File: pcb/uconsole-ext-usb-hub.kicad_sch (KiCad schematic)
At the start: 33 parts, among them J1 MINI_PCIE, P1 USB_C_Plug_USB2.0, P2 USB_C_Plug_USB2.0, P3 USB_C_Plug_USB2.0, P4 USB_C_Plug_USB2.0, U1 TUSB2048B, U2 TPS2044D, U3 USBLC6-2P6, U4 USBLC6-2P6, U5 USBLC6-2P6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

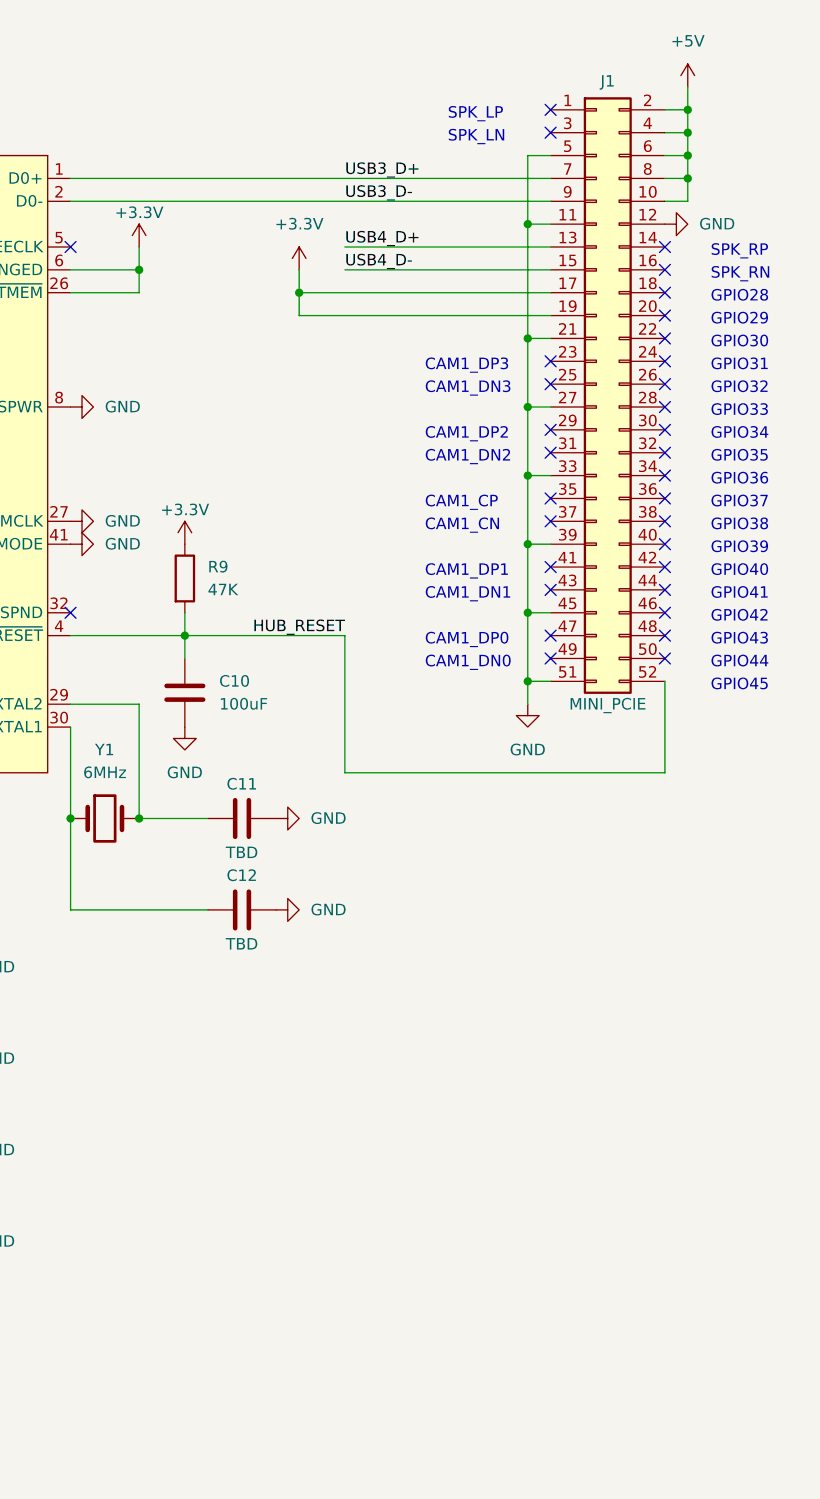
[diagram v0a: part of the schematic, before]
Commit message: sch: add speakers
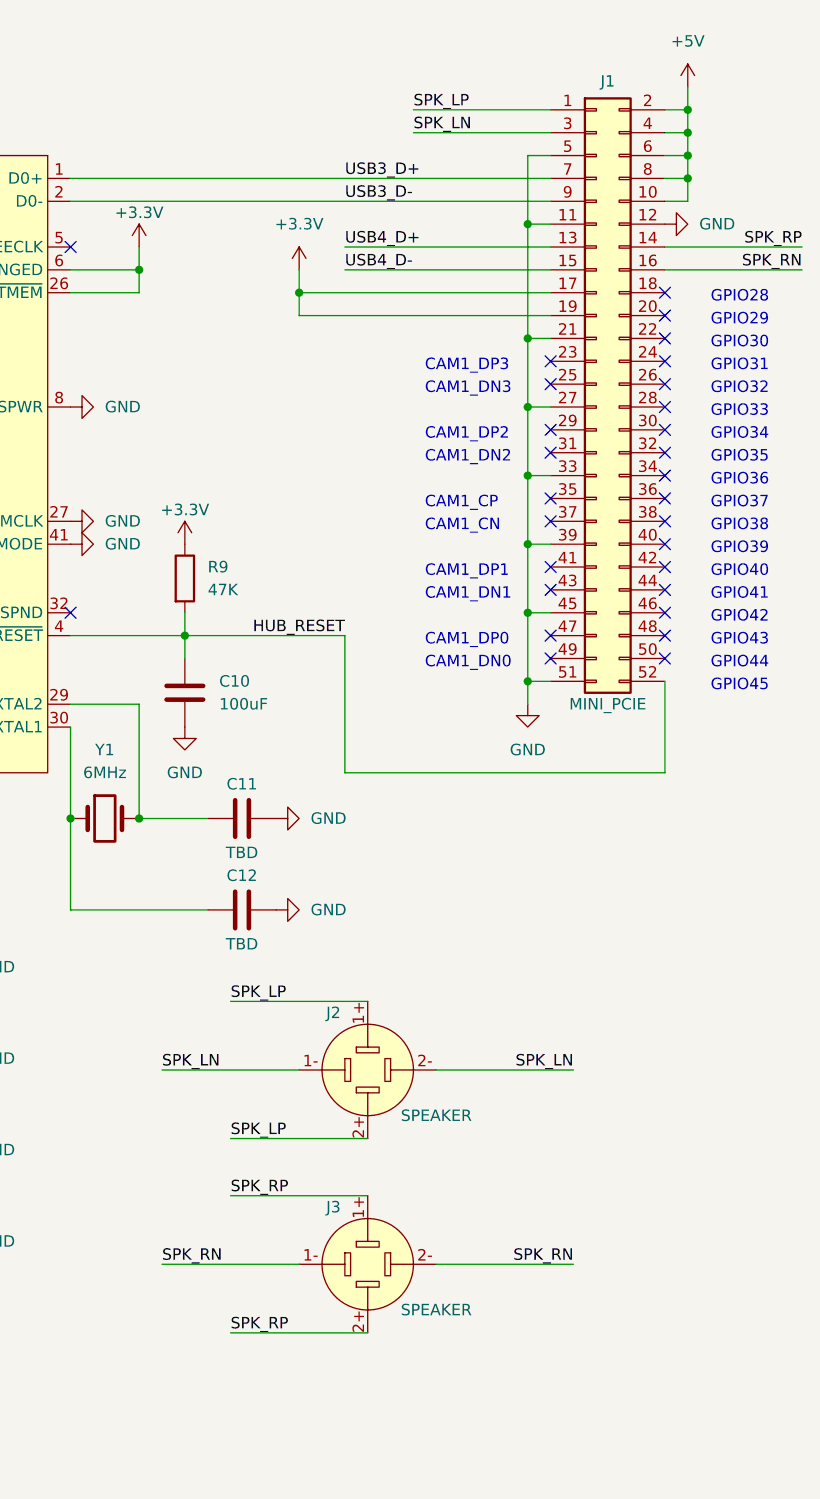
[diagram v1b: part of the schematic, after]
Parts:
- added J2, J3: SPEAKER, symbol Connector_Audio:SpeakON_NL4
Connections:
- net SPK_LP: now reaches J1.1 (Pin_1)
- net SPK_LP: now also J2.1+, J2.2+
- net SPK_RP: now reaches J1.14 (Pin_14)
- net SPK_RP: now also J3.1+, J3.2+
- net SPK_RN: now reaches J1.16 (Pin_16)
- net SPK_RN: now also J3.1-, J3.2-
- net SPK_LN: now reaches J1.3 (Pin_3)
- net SPK_LN: now also J2.1-, J2.2-
- no-connect marks 33 -> 29
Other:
- note removed: "SPK_LN"
- note removed: "SPK_LP"
- note removed: "SPK_RN"
- note removed: "SPK_RP"
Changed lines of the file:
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@@
   (title_block
     (title "uConsole Extension USB Hub")
-    (date "2023-07-21")
-    (rev "0.0.1")
+    (date "2023-07-22")
+    (rev "0.0.2")
     (company "by argrento")
     (comment 2 "https://codeberg.org/argrento/uconsole-ext-usb-hub")
@@
   (junction (at 254 86.36) (diameter 0) (color 0 0 0 0)
   )
-  (no_connect (at 269.24 40.64))
-  (no_connect (at 269.24 38.1))
   (no_connect (at 269.24 81.28))
   (no_connect (at 269.24 55.88))
@@
   (no_connect (at 256.54 68.58))
   (no_connect (at 256.54 60.96))
-  (no_connect (at 256.54 25.4))
   (no_connect (at 269.24 68.58))
-  (no_connect (at 256.54 22.86))
   (no_connect (at 269.24 63.5))
   (no_connect (at 269.24 83.82))
@@
     (stroke (width 0) (type default))
   )
+  (wire (pts (xy 241.3 25.4) (xy 256.54 25.4))
+    (stroke (width 0) (type default))
+  )
   (wire (pts (xy 165.1 91.44) (xy 165.1 165.1))
     (stroke (width 0) (type default))
@@
     (stroke (width 0) (type default))
   )
+  (wire (pts (xy 241.3 22.86) (xy 256.54 22.86))
+    (stroke (width 0) (type default))
+  )
   (wire (pts (xy 187.96 20.32) (xy 190.5 20.32))
     (stroke (width 0) (type default))
@@
     (stroke (width 0) (type default))
   )
+  (wire (pts (xy 259.08 151.13) (xy 243.84 151.13))
+    (stroke (width 0) (type default))
+  )
   (wire (pts (xy 53.34 128.27) (xy 39.37 128.27))
     (stroke (width 0) (type default))
@@
     (stroke (width 0) (type default))
   )
+  (wire (pts (xy 220.98 143.51) (xy 236.22 143.51))
+    (stroke (width 0) (type default))
+  )
   (wire (pts (xy 67.31 22.86) (xy 67.31 25.4))
     (stroke (width 0) (type default))
@@
     (stroke (width 0) (type default))
   )
+  (wire (pts (xy 284.48 40.64) (xy 269.24 40.64))
+    (stroke (width 0) (type default))
+  )
   (wire (pts (xy 203.2 91.44) (xy 203.2 101.6))
     (stroke (width 0) (type default))
@@
     (stroke (width 0) (type default))
   )
+  (wire (pts (xy 220.98 158.75) (xy 236.22 158.75))
+    (stroke (width 0) (type default))
+  )
   (wire (pts (xy 53.34 168.91) (xy 39.37 168.91))
     (stroke (width 0) (type default))
@@
     (stroke (width 0) (type default))
   )
+  (wire (pts (xy 213.36 129.54) (xy 228.6 129.54))
+    (stroke (width 0) (type default))
+  )
   (wire (pts (xy 254 35.56) (xy 254 48.26))
     (stroke (width 0) (type default))
@@
     (stroke (width 0) (type default))
   )
+  (wire (pts (xy 220.98 137.16) (xy 236.22 137.16))
+    (stroke (width 0) (type default))
+  )
   (wire (pts (xy 137.16 132.08) (xy 152.4 132.08))
     (stroke (width 0) (type default))
@@
     (stroke (width 0) (type default))
   )
+  (wire (pts (xy 213.36 151.13) (xy 228.6 151.13))
+    (stroke (width 0) (type default))
+  )
   (wire (pts (xy 24.13 194.31) (xy 31.75 194.31))
     (stroke (width 0) (type default))
   )
+  (wire (pts (xy 220.98 121.92) (xy 236.22 121.92))
+    (stroke (width 0) (type default))
+  )
   (wire (pts (xy 142.24 91.44) (xy 142.24 60.96))
     (stroke (width 0) (type default))
@@
     (stroke (width 0) (type default))
   )
+  (wire (pts (xy 259.08 129.54) (xy 243.84 129.54))
+    (stroke (width 0) (type default))
+  )
   (wire (pts (xy 116.84 91.44) (xy 142.24 91.44))
     (stroke (width 0) (type default))
@@
     (stroke (width 0) (type default))
   )
+  (wire (pts (xy 284.48 38.1) (xy 269.24 38.1))
+    (stroke (width 0) (type default))
+  )
   (text "CAM1_DN1" (at 242.57 77.47 0)
     (effects (font (size 1.27 1.27)) (justify left bottom))
@@
     (effects (font (size 1.27 1.27)) (justify left bottom))
   )
-  (text "SPK_RN" (at 274.32 41.91 0)
-    (effects (font (size 1.27 1.27)) (justify left bottom))
-  )
   (text "CAM1_DP3" (at 242.57 52.07 0)
     (effects (font (size 1.27 1.27)) (justify left bottom))
@@
     (effects (font (size 1.27 1.27)) (justify left bottom))
   )
-  (text "SPK_RP" (at 274.32 39.37 0)
-    (effects (font (size 1.27 1.27)) (justify left bottom))
-  )
   (text "GPIO38" (at 274.32 69.85 0)
     (effects (font (size 1.27 1.27)) (justify left bottom))
@@
     (effects (font (size 1.27 1.27)) (justify left bottom))
   )
-  (text "SPK_LP" (at 245.11 24.13 0)
-    (effects (font (size 1.27 1.27)) (justify left bottom))
-  )
   (text "GPIO36" (at 274.32 64.77 0)
     (effects (font (size 1.27 1.27)) (justify left bottom))
   )
   (text "GPIO35" (at 274.32 62.23 0)
-    (effects (font (size 1.27 1.27)) (justify left bottom))
-  )
-  (text "SPK_LN" (at 245.11 26.67 0)
     (effects (font (size 1.27 1.27)) (justify left bottom))
   )
@@
     (effects (font (size 1.27 1.27)) (justify right bottom))
   )
+  (label "SPK_RP" (at 220.98 143.51 0) (fields_autoplaced)
+    (effects (font (size 1.27 1.27)) (justify left bottom))
+  )
   (label "USB4_D-" (at 233.68 40.64 0) (fields_autoplaced)
     (effects (font (size 1.27 1.27)) (justify left bottom))
@@
     (effects (font (size 1.27 1.27)) (justify left bottom))
   )
+  (label "SPK_RP" (at 284.48 38.1 180) (fields_autoplaced)
+    (effects (font (size 1.27 1.27)) (justify right bottom))
+  )
   (label "USB1_D-" (at 91.44 35.56 0) (fields_autoplaced)
     (effects (font (size 1.27 1.27)) (justify left bottom))
@@
     (effects (font (size 1.27 1.27)) (justify left bottom))
   )
+  (label "SPK_LN" (at 213.36 129.54 0) (fields_autoplaced)
+    (effects (font (size 1.27 1.27)) (justify left bottom))
+  )
   (label "VBUS2" (at 172.72 128.27 0) (fields_autoplaced)
     (effects (font (size 1.27 1.27)) (justify left bottom))
   )
   (label "VBUS1" (at 172.72 118.11 0) (fields_autoplaced)
+    (effects (font (size 1.27 1.27)) (justify left bottom))
+  )
+  (label "SPK_LN" (at 259.08 129.54 180) (fields_autoplaced)
+    (effects (font (size 1.27 1.27)) (justify right bottom))
+  )
+  (label "SPK_RP" (at 220.98 158.75 0) (fields_autoplaced)
     (effects (font (size 1.27 1.27)) (justify left bottom))
   )
@@
     (effects (font (size 1.27 1.27)) (justify right bottom))
   )
+  (label "SPK_LP" (at 220.98 121.92 0) (fields_autoplaced)
+    (effects (font (size 1.27 1.27)) (justify left bottom))
+  )
   (label "VBUS2" (at 96.52 50.8 0) (fields_autoplaced)
     (effects (font (size 1.27 1.27)) (justify left bottom))
@@
     (effects (font (size 1.27 1.27)) (justify left bottom))
   )
+  (label "SPK_LN" (at 241.3 25.4 0) (fields_autoplaced)
+    (effects (font (size 1.27 1.27)) (justify left bottom))
+  )
   (label "VBUS1" (at 93.98 134.62 0) (fields_autoplaced)
+    (effects (font (size 1.27 1.27)) (justify left bottom))
+  )
+  (label "SPK_LP" (at 241.3 22.86 0) (fields_autoplaced)
     (effects (font (size 1.27 1.27)) (justify left bottom))
   )
@@
     (effects (font (size 1.27 1.27)) (justify right bottom))
   )
+  (label "SPK_RN" (at 259.08 151.13 180) (fields_autoplaced)
+    (effects (font (size 1.27 1.27)) (justify right bottom))
+  )
   (label "VBUS2" (at 93.98 137.16 0) (fields_autoplaced)
     (effects (font (size 1.27 1.27)) (justify left bottom))
@@
     (effects (font (size 1.27 1.27)) (justify left bottom))
   )
+  (label "SPK_RN" (at 213.36 151.13 0) (fields_autoplaced)
+    (effects (font (size 1.27 1.27)) (justify left bottom))
+  )
   (label "PWRON4" (at 147.32 177.8 180) (fields_autoplaced)
     (effects (font (size 1.27 1.27)) (justify right bottom))
   )
+  (label "SPK_LP" (at 220.98 137.16 0) (fields_autoplaced)
+    (effects (font (size 1.27 1.27)) (justify left bottom))
+  )
   (label "USB4_D+" (at 91.44 91.44 0) (fields_autoplaced)
     (effects (font (size 1.27 1.27)) (justify left bottom))
@@
   (label "VBUS4" (at 172.72 148.59 0) (fields_autoplaced)
     (effects (font (size 1.27 1.27)) (justify left bottom))
+  )
+  (label "SPK_RN" (at 284.48 40.64 180) (fields_autoplaced)
+    (effects (font (size 1.27 1.27)) (justify right bottom))
   )
   (label "USB2_D-" (at 53.34 76.2 180) (fields_autoplaced)
@@
     )
   )
+  (symbol (lib_id "Connector_Audio:SpeakON_NL4") (at 236.22 129.54 0) (unit 1)
+    (in_bom yes) (on_board yes) (dnp no)
+    (property "Reference" "J2" (at 232.41 123.19 0)
+      (effects (font (size 1.27 1.27)))
+    )
+    (property "Value" "SPEAKER" (at 243.84 134.62 0)
+      (effects (font (size 1.27 1.27)))
+    )
+    (property "Footprint" "" (at 236.22 129.54 0)
+      (effects (font (size 1.27 1.27)) hide)
+    )
+    (property "Datasheet" "" (at 236.22 129.54 0)
+      (effects (font (size 1.27 1.27)) hide)
+    )
+    (pin "1-")
+    (pin "2+")
+    (pin "2-")
+    (pin "1+")
+    (instances
+      (project "uconsole-ext-usb-hub"
+        (path "/f960929c-7fdd-4df6-ba15-306cc765424b"
+          (reference "J2") (unit 1)
+        )
+      )
+    )
+  )
   (symbol (lib_id "Device:R") (at 58.42 74.93 0) (unit 1)
     (in_bom yes) (on_board yes) (dnp no) (fields_autoplaced)
@@
         )
       )
+    )
+  )
+  (symbol (lib_id "Connector_Audio:SpeakON_NL4") (at 236.22 151.13 0) (unit 1)
+    (in_bom yes) (on_board yes) (dnp no)
+    (property "Reference" "J3" (at 232.41 144.78 0)
+      (effects (font (size 1.27 1.27)))
+    )
+    (property "Value" "SPEAKER" (at 243.84 156.21 0)
+      (effects (font (size 1.27 1.27)))
+    )
+    (property "Footprint" "" (at 236.22 151.13 0)
+      (effects (font (size 1.27 1.27)) hide)
+    )
+    (property "Datasheet" "" (at 236.22 151.13 0)
+      (effects (font (size 1.27 1.27)) hide)
+    )
+    (pin "1-")
+    (pin "2+")
+    (pin "2-")
+    (pin "1+")
+    (instances
+      (project "uconsole-ext-usb-hub"
+        (path "/f960929c-7fdd-4df6-ba15-306cc765424b"
+          (reference "J3") (unit 1)
+        )
+      )

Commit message: First PCB version
* Added speakers
* Initial pcb
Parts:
- removed J2, J3: SPEAKER, symbol Connector_Audio:SpeakON_NL4
- removed Y1: 6MHz, symbol Device:Crystal
- added J2, J3: SPEAKER, custom_components:uConsole_speaker, symbol Connector_Generic:Conn_02x02_Counter_Clockwise
- added Y1: 6MHz, Crystal:Crystal_SMD_2016-4Pin_2.0x1.6mm, symbol Device:Crystal_GND24
- C11, C12, C5, C6, C7, C8, C9: footprint (none) -> Capacitor_SMD:C_0603_1608Metric
- J1: footprint (none) -> custom_components:mini_pcie_edge
- P1, P2, P3, P4: footprint (none) -> Connector_USB:USB_C_Receptacle_GCT_USB4105-xx-A_16P_TopMnt_Horizontal
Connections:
- net GND: now also U1.31 (TSTMODE), Y1.2, Y1.4; no longer U1.41 (TSTMODE)
- net HUB_RESET: now also J1.18 (Pin_18); no longer J1.52 (Pin_52)
- net PWRON2: now also U1.13 (~{PWRON2}); no longer U1.12 (~{PWRON2})
- net SPK_LN: now also J3.2 (Pin_2), J3.4 (Pin_4)
- net SPK_LP: now also J3.1 (Pin_1), J3.3 (Pin_3)
- net SPK_RN: now also J2.2 (Pin_2), J2.4 (Pin_4)
- net SPK_RP: now also J2.1 (Pin_1), J2.3 (Pin_3)
- net USB1_D+: now also U3.6 (I/O1); no longer U3.4 (I/O2)
- net USB1_D-: now also U3.4 (I/O2); no longer U3.6 (I/O1)
- net USB2_D+: now also U4.6 (I/O1); no longer U4.4 (I/O2)
- net USB2_D-: now also U4.4 (I/O2); no longer U4.6 (I/O1)
- net USB3_D+: now also U5.6 (I/O1); no longer J1.7 (Pin_7), U1.1 (D0+), U5.4 (I/O2)
- net USB3_D-: now also U5.4 (I/O2); no longer J1.9 (Pin_9), U1.2 (D0-), U5.6 (I/O1)
- net USB4_D+: now also U6.6 (I/O1); no longer J1.13 (Pin_13), U6.4 (I/O2)
- net USB4_D-: now also U6.4 (I/O2); no longer J1.15 (Pin_15), U6.6 (I/O1)
- net USBH1_D+: now also U3.1 (I/O1); no longer U3.3 (I/O2)
- net USBH1_D-: now also U3.3 (I/O2); no longer U3.1 (I/O1)
- net USBH2_D+: now also U4.1 (I/O1); no longer U4.3 (I/O2)
- net USBH2_D-: now also U4.3 (I/O2); no longer U4.1 (I/O1)
- net USBH3_D+: now also U5.1 (I/O1); no longer U5.3 (I/O2)
- net USBH3_D-: now also U5.3 (I/O2); no longer U5.1 (I/O1)
- net USBH4_D+: now also U6.1 (I/O1); no longer U6.3 (I/O2)
- net USBH4_D-: now also U6.3 (I/O2); no longer U6.1 (I/O1)
- net at C11.1, U1.29 (XTAL2): now also Y1.3
- net at C12.1, U1.30 (XTAL1): now also Y1.1
- new net EXT_USB3_D+: J1.7 (Pin_7), U1.1 (D0+)
- new net EXT_USB3_D-: J1.9 (Pin_9), U1.2 (D0-)
- new net EXT_USB4_D+: J1.13 (Pin_13)
- new net EXT_USB4_D-: J1.15 (Pin_15)
